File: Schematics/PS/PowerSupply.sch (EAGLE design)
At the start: 78 parts, among them IC1 LM317MABDT, IC2 LM337, T1 IRFP240, T2 IRFP240

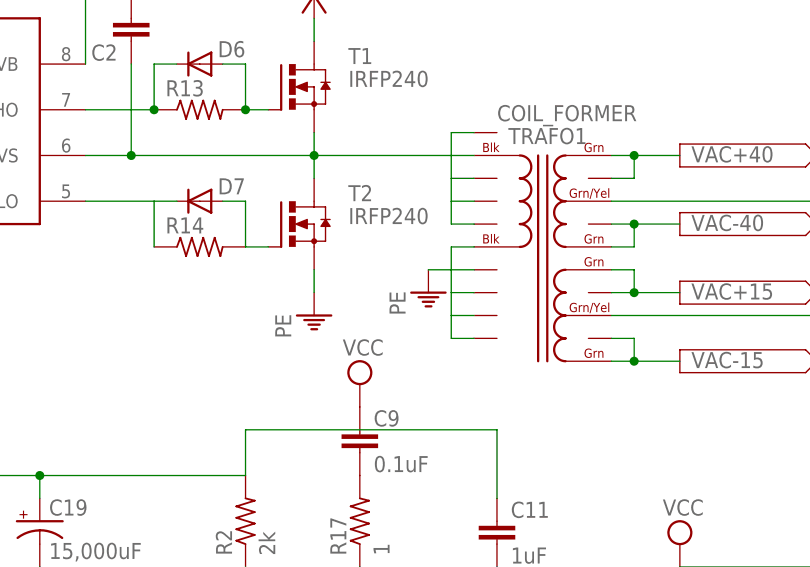
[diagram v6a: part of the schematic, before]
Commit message: added DC blocking cap on trafo
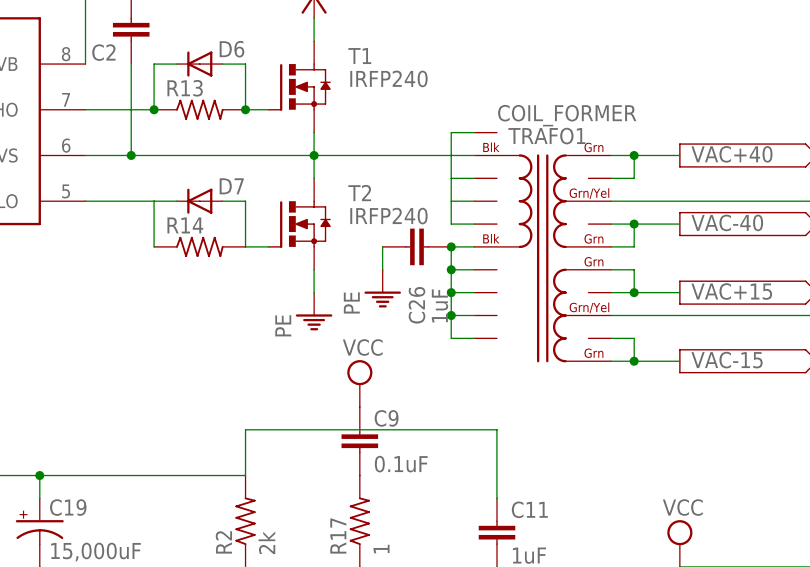
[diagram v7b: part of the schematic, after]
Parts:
- added C26: 1uF, resistor:C-EU025-025X050
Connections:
- new net N$9: C26.2, TRAFO1.P2, TRAFO1.P22, TRAFO1.P23, TRAFO1.P24, TRAFO1.P25
- net GND: now also C26.1; no longer TRAFO1.P2, TRAFO1.P22, TRAFO1.P23, TRAFO1.P24, TRAFO1.P25
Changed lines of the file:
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@@
 <part name="C14" library="rcl" deviceset="CPOL-EU" device="E2.5-6" value="1uF"/>
 <part name="C25" library="rcl" deviceset="CPOL-EU" device="E2.5-6" value="1uF"/>
+<part name="C26" library="resistor" deviceset="C-EU" device="025-025X050" value="1uF"/>
 </parts>
 <sheets>
@@
 <instance part="R14" gate="G$1" x="129.54" y="50.8"/>
 <instance part="TRAFO1" gate="G$1" x="167.64" y="55.88"/>
-<instance part="PE13" gate="M" x="154.94" y="45.72"/>
+<instance part="PE13" gate="M" x="149.86" y="45.72"/>
 <instance part="SUPPLY4" gate="1" x="142.24" y="78.74"/>
 <instance part="PE14" gate="M" x="142.24" y="43.18"/>
@@
 <attribute name="VALUE" x="174.244" y="-60.579" size="1.778" layer="96"/>
 </instance>
+<instance part="C26" gate="G$1" x="152.4" y="50.8" smashed="yes" rot="R90">
+<attribute name="NAME" x="154.559" y="42.164" size="1.778" layer="95" rot="R90"/>
+<attribute name="VALUE" x="157.099" y="42.164" size="1.778" layer="96" rot="R90"/>
+</instance>
 </instances>
 <busses>
@@
 </segment>
 <segment>
-<pinref part="TRAFO1" gate="G$1" pin="P22"/>
-<pinref part="PE13" gate="M" pin="PE"/>
-<wire x1="154.94" y1="48.26" x2="157.48" y2="48.26" width="0.1524" layer="91"/>
-<pinref part="TRAFO1" gate="G$1" pin="P2"/>
-<wire x1="157.48" y1="48.26" x2="160.02" y2="48.26" width="0.1524" layer="91"/>
-<wire x1="160.02" y1="50.8" x2="157.48" y2="50.8" width="0.1524" layer="91"/>
-<wire x1="157.48" y1="50.8" x2="157.48" y2="48.26" width="0.1524" layer="91"/>
-<wire x1="157.48" y1="48.26" x2="157.48" y2="45.72" width="0.1524" layer="91"/>
-<pinref part="TRAFO1" gate="G$1" pin="P23"/>
-<wire x1="160.02" y1="45.72" x2="157.48" y2="45.72" width="0.1524" layer="91"/>
-<wire x1="157.48" y1="45.72" x2="157.48" y2="43.18" width="0.1524" layer="91"/>
-<pinref part="TRAFO1" gate="G$1" pin="P24"/>
-<wire x1="160.02" y1="43.18" x2="157.48" y2="43.18" width="0.1524" layer="91"/>
-<wire x1="157.48" y1="43.18" x2="157.48" y2="40.64" width="0.1524" layer="91"/>
-<pinref part="TRAFO1" gate="G$1" pin="P25"/>
-<wire x1="157.48" y1="40.64" x2="160.02" y2="40.64" width="0.1524" layer="91"/>
-</segment>
-<segment>
 <pinref part="U$5" gate="G$1" pin="COM"/>
 <wire x1="88.9" y1="55.88" x2="86.36" y2="55.88" width="0.1524" layer="91"/>
@@
 <pinref part="PE7" gate="M" pin="PE"/>
 <wire x1="-17.78" y1="76.2" x2="-15.24" y2="76.2" width="0.1524" layer="91"/>
+</segment>
+<segment>
+<pinref part="C26" gate="G$1" pin="1"/>
+<pinref part="PE13" gate="M" pin="PE"/>
+<wire x1="149.86" y1="50.8" x2="149.86" y2="48.26" width="0.1524" layer="91"/>
 </segment>
 </net>
@@
 </segment>
 </net>
+<net name="N$9" class="0">
+<segment>
+<pinref part="TRAFO1" gate="G$1" pin="P2"/>
+<pinref part="C26" gate="G$1" pin="2"/>
+<wire x1="157.48" y1="50.8" x2="160.02" y2="50.8" width="0.1524" layer="91"/>
+<pinref part="TRAFO1" gate="G$1" pin="P25"/>
+<wire x1="160.02" y1="40.64" x2="157.48" y2="40.64" width="0.1524" layer="91"/>
+<wire x1="157.48" y1="40.64" x2="157.48" y2="43.18" width="0.1524" layer="91"/>
+<wire x1="157.48" y1="50.8" x2="157.48" y2="48.26" width="0.1524" layer="91"/>
+<pinref part="TRAFO1" gate="G$1" pin="P22"/>
+<wire x1="160.02" y1="48.26" x2="157.48" y2="48.26" width="0.1524" layer="91"/>
+<wire x1="157.48" y1="48.26" x2="157.48" y2="45.72" width="0.1524" layer="91"/>
+<pinref part="TRAFO1" gate="G$1" pin="P23"/>
+<wire x1="160.02" y1="45.72" x2="157.48" y2="45.72" width="0.1524" layer="91"/>
+<wire x1="157.48" y1="45.72" x2="157.48" y2="43.18" width="0.1524" layer="91"/>
+<pinref part="TRAFO1" gate="G$1" pin="P24"/>
+<wire x1="157.48" y1="43.18" x2="160.02" y2="43.18" width="0.1524" layer="91"/>
+<junction x="157.48" y="43.18"/>
+<junction x="157.48" y="45.72"/>
+<junction x="157.48" y="48.26"/>
+<junction x="157.48" y="50.8"/>
+</segment>
+</net>

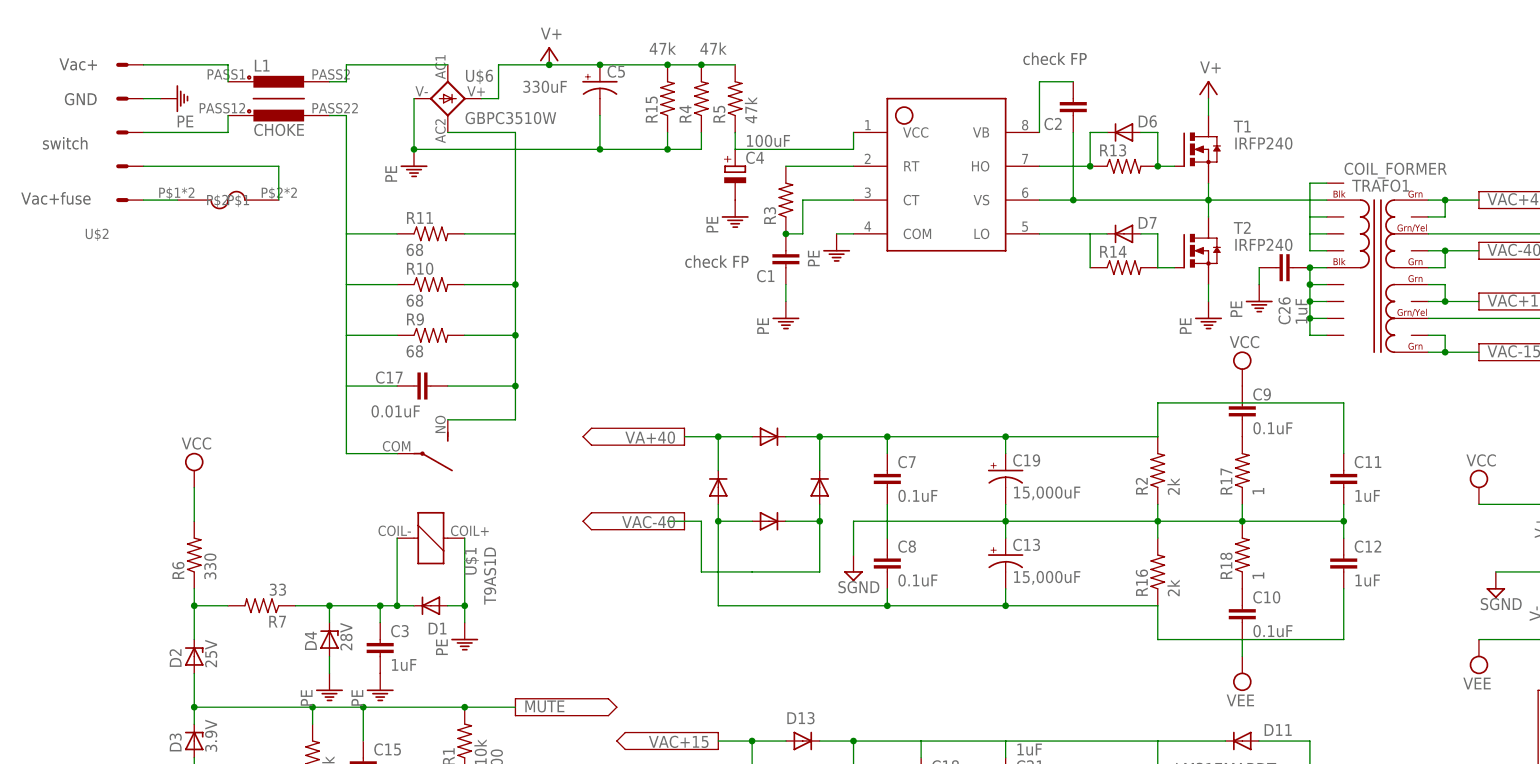
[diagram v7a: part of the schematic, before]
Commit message: updates to PS, fixed GND issue
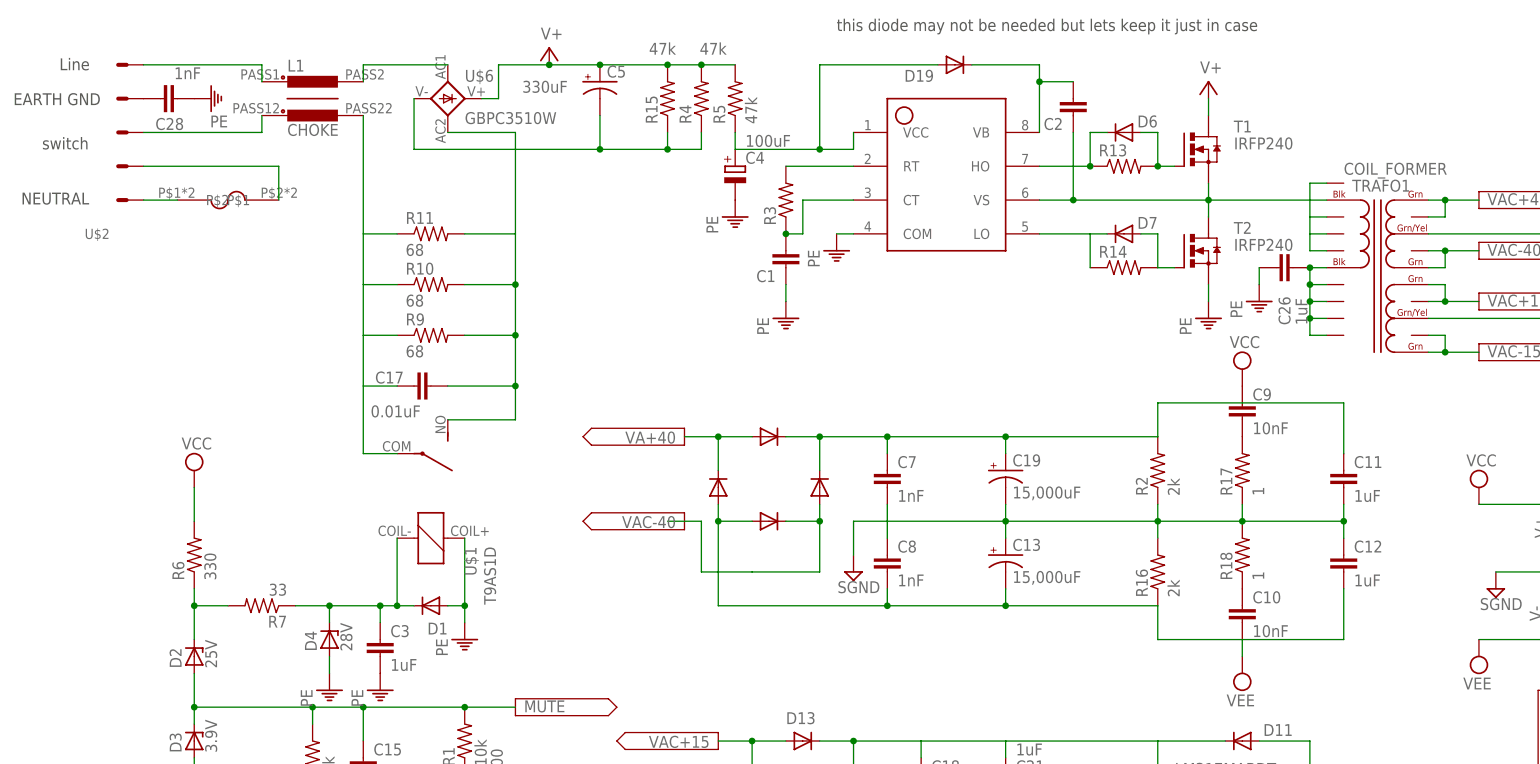
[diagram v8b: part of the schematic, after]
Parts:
- added C28: 1nF, rcl:C-EU102-064X133
- added D19: 1N4004, Amplifier_Parts:1N4004
- C10, C9: value 0.1uF -> 10nF
- C7, C8: value 0.1uF -> 1nF
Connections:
- new net N$12: C28.1, U$2.S4
- net GND: now also C28.2; no longer U$2.S4
- net N$17: now also D19.A
- net N$6: now also D19.C
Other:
- note added: "EARTH GND"
- note added: "Line"
- note added: "NEUTRAL"
- note added: "this diode may not be needed but lets keep it just in case"
- note removed: "GND"
- note removed: "Vac+"
- note removed: "Vac+fuse"
- note removed: "check FP"
- moved on the sheet: L1
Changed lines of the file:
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@@
 <part name="C4" library="rcl" deviceset="CPOL-EU" device="E2.5-6" value="100uF"/>
 <part name="PE9" library="supply1" deviceset="PE" device=""/>
-<part name="PE10" library="supply1" deviceset="PE" device=""/>
 <part name="PE11" library="supply1" deviceset="PE" device=""/>
 <part name="PE12" library="supply1" deviceset="PE" device=""/>
@@
 <part name="R17" library="rcl" deviceset="R-US_" device="0411/12" value="1"/>
 <part name="R18" library="rcl" deviceset="R-US_" device="0411/12" value="1"/>
-<part name="C7" library="rcl" deviceset="C-EU" device="102-064X133" value="0.1uF"/>
-<part name="C8" library="rcl" deviceset="C-EU" device="102-064X133" value="0.1uF"/>
-<part name="C9" library="rcl" deviceset="C-EU" device="102-064X133" value="0.1uF"/>
-<part name="C10" library="rcl" deviceset="C-EU" device="102-064X133" value="0.1uF"/>
+<part name="C7" library="rcl" deviceset="C-EU" device="102-064X133" value="1nF"/>
+<part name="C8" library="rcl" deviceset="C-EU" device="102-064X133" value="1nF"/>
+<part name="C9" library="rcl" deviceset="C-EU" device="102-064X133" value="10nF"/>
+<part name="C10" library="rcl" deviceset="C-EU" device="102-064X133" value="10nF"/>
 <part name="C19" library="Amplifier_Parts" deviceset="LNR1K153MSE" device="" value="15,000uF"/>
 <part name="SUPPLY11" library="supply2" deviceset="VCC" device=""/>
@@
 <part name="C25" library="rcl" deviceset="CPOL-EU" device="E2.5-6" value="1uF"/>
 <part name="C26" library="resistor" deviceset="C-EU" device="025-025X050" value="1uF"/>
+<part name="C28" library="rcl" deviceset="C-EU" device="102-064X133" value="1nF"/>
+<part name="D19" library="Amplifier_Parts" deviceset="1N4004" device=""/>
 </parts>
 <sheets>
 <sheet>
 <plain>
-<text x="-30.4336625" y="80.47009375" size="1.778" layer="97">Vac+</text>
-<text x="-29.729371875" y="75.2281125" size="1.778" layer="97">GND</text>
-<text x="-36.1696" y="60.2996" size="1.778" layer="97">Vac+fuse</text>
+<text x="-30.4336625" y="80.47009375" size="1.778" layer="97">Line</text>
+<text x="-37.349371875" y="75.2281125" size="1.778" layer="97">EARTH GND</text>
+<text x="-36.1696" y="60.2996" size="1.778" layer="97">NEUTRAL</text>
 <text x="-33.02" y="68.58" size="1.778" layer="97">switch</text>
-<text x="63.5" y="50.8" size="1.778" layer="97">check FP</text>
-<text x="114.3" y="81.28" size="1.778" layer="97">check FP</text>
+<text x="86.36" y="86.36" size="1.778" layer="97">this diode may not be needed but lets keep it just in case</text>
 </plain>
 <instances>
@@
 <instance part="C1" gate="G$1" x="78.74" y="50.8" rot="R180"/>
 <instance part="U$6" gate="G$1" x="27.94" y="76.2"/>
-<instance part="L1" gate="G$1" x="2.54" y="76.2"/>
-<instance part="PE7" gate="M" x="-12.7" y="76.2" rot="R90"/>
+<instance part="L1" gate="G$1" x="7.62" y="76.2"/>
+<instance part="PE7" gate="M" x="-7.62" y="76.2" rot="R90"/>
 <instance part="C4" gate="G$1" x="71.12" y="66.04" smashed="yes">
 <attribute name="NAME" x="72.644" y="66.421" size="1.778" layer="95"/>
@@
 </instance>
 <instance part="PE9" gate="M" x="71.12" y="58.42"/>
-<instance part="PE10" gate="M" x="22.86" y="66.04"/>
 <instance part="PE11" gate="M" x="86.36" y="53.34"/>
 <instance part="PE12" gate="M" x="78.74" y="43.18"/>
@@
 <attribute name="VALUE" x="157.099" y="42.164" size="1.778" layer="96" rot="R90"/>
 </instance>
+<instance part="C28" gate="G$1" x="-15.24" y="76.2" smashed="yes" rot="R90">
+<attribute name="NAME" x="-11.684" y="73.279" size="1.778" layer="95" rot="R180"/>
+<attribute name="VALUE" x="-9.144" y="80.899" size="1.778" layer="96" rot="R180"/>
+</instance>
+<instance part="D19" gate="G$1" x="104.14" y="81.28" smashed="yes">
+<attribute name="NAME" x="96.52" y="78.74" size="1.778" layer="95"/>
+</instance>
 </instances>
 <busses>
@@
 </segment>
 <segment>
-<wire x1="12.7" y1="55.88" x2="12.7" y2="48.26" width="0.1524" layer="91"/>
-<wire x1="12.7" y1="48.26" x2="12.7" y2="40.64" width="0.1524" layer="91"/>
-<wire x1="12.7" y1="40.64" x2="12.7" y2="33.02" width="0.1524" layer="91"/>
-<wire x1="12.7" y1="33.02" x2="12.7" y2="22.86" width="0.1524" layer="91"/>
+<wire x1="15.24" y1="55.88" x2="15.24" y2="48.26" width="0.1524" layer="91"/>
+<wire x1="15.24" y1="48.26" x2="15.24" y2="40.64" width="0.1524" layer="91"/>
+<wire x1="15.24" y1="40.64" x2="15.24" y2="33.02" width="0.1524" layer="91"/>
+<wire x1="15.24" y1="33.02" x2="15.24" y2="22.86" width="0.1524" layer="91"/>
 <pinref part="R11" gate="G$1" pin="1"/>
-<wire x1="20.32" y1="55.88" x2="12.7" y2="55.88" width="0.1524" layer="91"/>
+<wire x1="20.32" y1="55.88" x2="15.24" y2="55.88" width="0.1524" layer="91"/>
 <pinref part="R10" gate="G$1" pin="1"/>
-<wire x1="20.32" y1="48.26" x2="12.7" y2="48.26" width="0.1524" layer="91"/>
+<wire x1="20.32" y1="48.26" x2="15.24" y2="48.26" width="0.1524" layer="91"/>
 <pinref part="R9" gate="G$1" pin="1"/>
-<wire x1="12.7" y1="40.64" x2="20.32" y2="40.64" width="0.1524" layer="91"/>
+<wire x1="15.24" y1="40.64" x2="20.32" y2="40.64" width="0.1524" layer="91"/>
 <pinref part="C17" gate="G$1" pin="1"/>
-<wire x1="20.32" y1="33.02" x2="12.7" y2="33.02" width="0.1524" layer="91"/>
+<wire x1="20.32" y1="33.02" x2="15.24" y2="33.02" width="0.1524" layer="91"/>
 <pinref part="U$1" gate="G$1" pin="COM"/>
-<wire x1="12.7" y1="22.86" x2="20.32" y2="22.86" width="0.1524" layer="91"/>
+<wire x1="15.24" y1="22.86" x2="20.32" y2="22.86" width="0.1524" layer="91"/>
 <pinref part="L1" gate="G$1" pin="W2E"/>
-<wire x1="10.16" y1="73.66" x2="12.7" y2="73.66" width="0.1524" layer="91"/>
-<wire x1="12.7" y1="73.66" x2="12.7" y2="55.88" width="0.1524" layer="91"/>
+<wire x1="15.24" y1="73.66" x2="15.24" y2="55.88" width="0.1524" layer="91"/>
 </segment>
 <segment>
@@
 <wire x1="60.96" y1="68.58" x2="66.04" y2="68.58" width="0.1524" layer="91"/>
 <wire x1="66.04" y1="68.58" x2="66.04" y2="71.12" width="0.1524" layer="91"/>
-<pinref part="PE10" gate="M" pin="PE"/>
-<junction x="22.86" y="68.58"/>
 <junction x="50.8" y="68.58"/>
 <junction x="60.96" y="68.58"/>
@@
 </segment>
 <segment>
-<pinref part="U$2" gate="G$1" pin="S4"/>
-<pinref part="PE7" gate="M" pin="PE"/>
-<wire x1="-17.78" y1="76.2" x2="-15.24" y2="76.2" width="0.1524" layer="91"/>
-</segment>
-<segment>
 <pinref part="C26" gate="G$1" pin="1"/>
 <pinref part="PE13" gate="M" pin="PE"/>
 <wire x1="149.86" y1="50.8" x2="149.86" y2="48.26" width="0.1524" layer="91"/>
+</segment>
+<segment>
+<pinref part="PE7" gate="M" pin="PE"/>
+<pinref part="C28" gate="G$1" pin="2"/>
 </segment>
 </net>
@@
 <segment>
 <pinref part="U$2" gate="G$1" pin="S5"/>
-<wire x1="-17.78" y1="81.28" x2="-5.08" y2="81.28" width="0.1524" layer="91"/>
+<wire x1="-17.78" y1="81.28" x2="0" y2="81.28" width="0.1524" layer="91"/>
 <pinref part="L1" gate="G$1" pin="W1A"/>
-<wire x1="-5.08" y1="81.28" x2="-5.08" y2="78.74" width="0.1524" layer="91"/>
+<wire x1="0" y1="81.28" x2="0" y2="78.74" width="0.1524" layer="91"/>
 </segment>
 </net>
@@
 <segment>
 <pinref part="L1" gate="G$1" pin="W2A"/>
-<wire x1="-5.08" y1="73.66" x2="-5.08" y2="71.12" width="0.1524" layer="91"/>
+<wire x1="0" y1="73.66" x2="0" y2="71.12" width="0.1524" layer="91"/>
 <pinref part="U$2" gate="G$1" pin="S3"/>
-<wire x1="-5.08" y1="71.12" x2="-17.78" y2="71.12" width="0.1524" layer="91"/>
+<wire x1="0" y1="71.12" x2="-17.78" y2="71.12" width="0.1524" layer="91"/>
 </segment>
 </net>
@@
 <wire x1="116.84" y1="78.74" x2="121.92" y2="78.74" width="0.1524" layer="91"/>
 <pinref part="C2" gate="G$1" pin="2"/>
+<pinref part="D19" gate="G$1" pin="C"/>
+<wire x1="106.68" y1="81.28" x2="116.84" y2="81.28" width="0.1524" layer="91"/>
+<wire x1="116.84" y1="81.28" x2="116.84" y2="78.74" width="0.1524" layer="91"/>
+<junction x="116.84" y="78.74"/>
 </segment>
 </net>
@@
 </segment>
 </net>
-<net name="N$4" class="0">
-<segment>
-<pinref part="L1" gate="G$1" pin="W1E"/>
-<wire x1="10.16" y1="78.74" x2="12.7" y2="78.74" width="0.1524" layer="91"/>
-<wire x1="12.7" y1="78.74" x2="12.7" y2="81.28" width="0.1524" layer="91"/>
-<pinref part="U$6" gate="G$1" pin="AC1"/>
-<wire x1="12.7" y1="81.28" x2="27.94" y2="81.28" width="0.1524" layer="91"/>
-</segment>
-</net>
 <net name="N$17" class="0">
 <segment>
@@
 <wire x1="71.12" y1="71.12" x2="71.12" y2="68.58" width="0.1524" layer="91"/>
 <pinref part="U$5" gate="G$1" pin="VCC"/>
-<wire x1="71.12" y1="68.58" x2="88.9" y2="68.58" width="0.1524" layer="91"/>
+<wire x1="71.12" y1="68.58" x2="83.82" y2="68.58" width="0.1524" layer="91"/>
+<wire x1="83.82" y1="68.58" x2="88.9" y2="68.58" width="0.1524" layer="91"/>
 <wire x1="88.9" y1="68.58" x2="88.9" y2="71.12" width="0.1524" layer="91"/>
+<pinref part="D19" gate="G$1" pin="A"/>
+<wire x1="101.6" y1="81.28" x2="83.82" y2="81.28" width="0.1524" layer="91"/>
+<wire x1="83.82" y1="81.28" x2="83.82" y2="68.58" width="0.1524" layer="91"/>
+<junction x="83.82" y="68.58"/>
 </segment>
 </net>
@@
 </segment>
 </net>
+<net name="N$4" class="0">
+<segment>
+<pinref part="U$6" gate="G$1" pin="AC1"/>
+<pinref part="L1" gate="G$1" pin="W1E"/>
+<wire x1="27.94" y1="81.28" x2="15.24" y2="81.28" width="0.1524" layer="91"/>
+<wire x1="15.24" y1="81.28" x2="15.24" y2="78.74" width="0.1524" layer="91"/>
+</segment>
+</net>
+<net name="N$12" class="0">
+<segment>
+<pinref part="U$2" gate="G$1" pin="S4"/>
+<pinref part="C28" gate="G$1" pin="1"/>
+</segment>
+</net>
